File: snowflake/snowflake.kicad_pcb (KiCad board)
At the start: 2 copper layers, 150.2 x 150.2 mm, 82 parts, among them J1 Conn_01x05_Pin, J2 Conn_01x04_Pin, U1 TZ-5050S2RGB-5V-I4-H1, U10 TZ-5050S2RGB-5V-I4-H1, U11 TZ-5050S2RGB-5V-I4-H1, U12 TZ-5050S2RGB-5V-I4-H1, U13 TZ-5050S2RGB-5V-I4-H1, U14 TZ-5050S2RGB-5V-I4-H1, U15 TZ-5050S2RGB-5V-I4-H1, U16 TZ-5050S2RGB-5V-I4-H1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

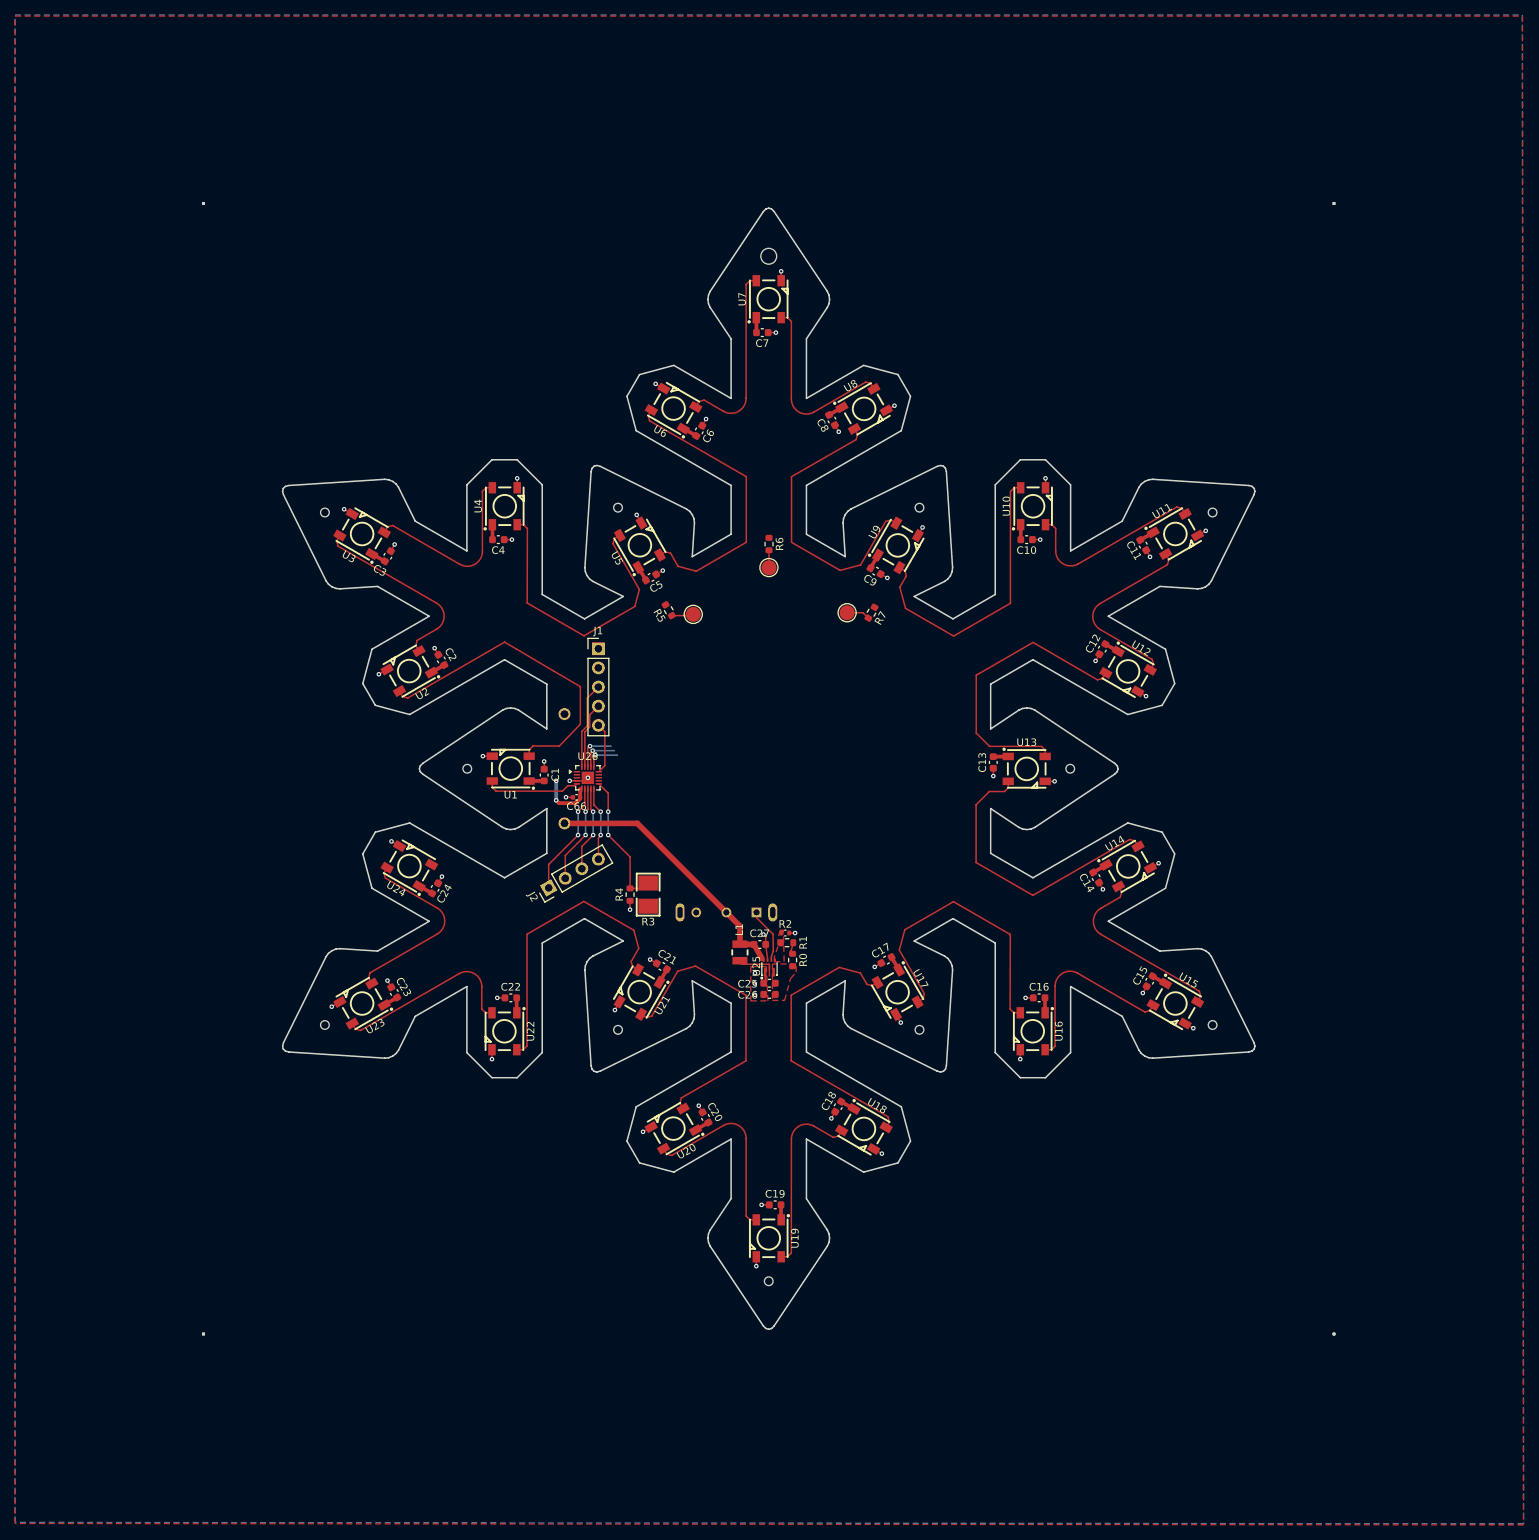
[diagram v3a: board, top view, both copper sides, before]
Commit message: Update PCB and customize some footprints
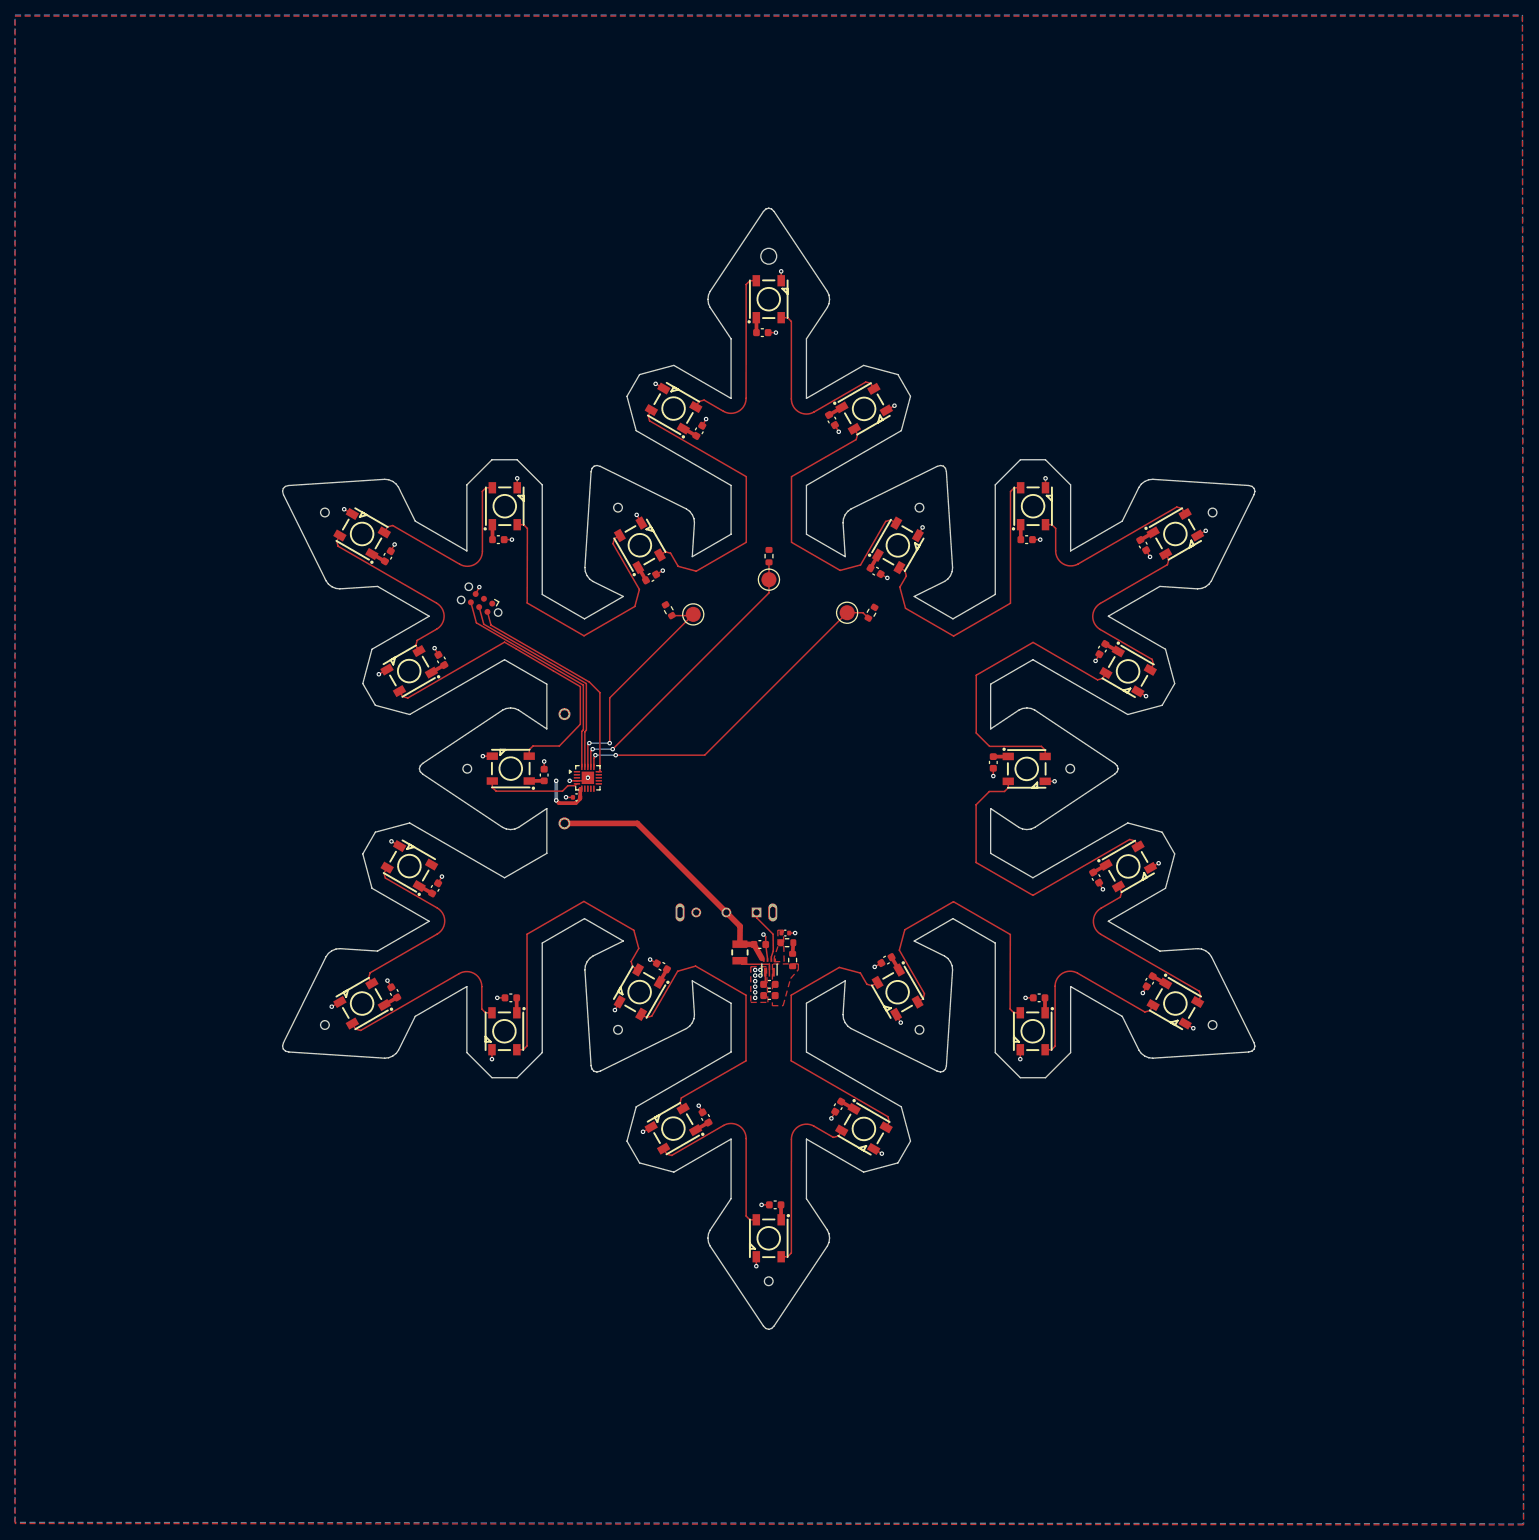
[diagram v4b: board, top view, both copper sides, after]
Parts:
- removed J1: Conn_01x05_Pin, Connector_PinHeader_2.54mm:PinHeader_1x05_P2.54mm_Vertical
- removed J2: Conn_01x04_Pin, Connector_PinHeader_2.54mm:PinHeader_1x04_P2.54mm_Vertical
- removed R3: C2904881, easyeda2kicad:RES-SMD_L3.6-W2.4
- removed R4: 10k, Resistor_SMD:R_0603_1608Metric
- added J3: TC2030, Connector:Tag-Connect_TC2030-IDC-NL_2x03_P1.27mm_Vertical, F.Cu at (111.9, 128.0)
- BAT1: footprint easyeda2kicad:BAT-TH_2P-P14.50_2462 -> snowflake:BAT-TH_2P-P14.50_2462
- C66: footprint Capacitor_SMD:C_0402_1005Metric -> snowflake:C_0402_1005Metric
- TP5, TP6, TP7: footprint TestPoint:TestPoint_Pad_D2.0mm -> snowflake:TestPoint_Pad_D2.0mm
- U25: footprint easyeda2kicad:VQFN-7_L2.0-W2.0-P0.55-TL_RWU -> snowflake:VQFN-7_L2.0-W2.0-P0.55-TL_RWU
- moved R6 1.60 mm to (150.0, 121.8)
- moved TP6 1.60 mm to (150.0, 124.9)
- moved C25 0.15 mm to (150.1, 178.6)
- moved C26 0.15 mm to (150.1, 180.1)
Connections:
- U26 pad 10: Net-(J2-Pin_4) -> unconnected-(U26-PC3/T1CH3-Pad10)
- U26 pad 11: /LDR_DIV -> unconnected-(U26-PC4/A2-Pad11)
- U26 pad 7: Net-(J2-Pin_1) -> unconnected-(U26-PC0/T2CH3-Pad7)
- U26 pad 8: Net-(J2-Pin_2) -> unconnected-(U26-PC1/SDA-Pad8)
- U26 pad 9: Net-(J2-Pin_3) -> unconnected-(U26-PC2/SCL-Pad9)
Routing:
- net /TOUCH3: track 7.33 -> 45.6 mm, vias 1 -> 2
- net /TOUCH2: track 8.28 -> 39.4 mm, vias 1 -> 2
- net /SWIO: track 6.84 -> 29.4 mm
- net /TOUCH1: track 8.64 -> 30.6 mm, vias 1 -> 2
- net /RX: track 8.80 -> 29.2 mm
- net /TX: track 11.5 -> 30.2 mm
- net /LDR_DIV: track 18.4 -> 0.00 mm, vias 2 -> 0
- net Net-(J2-Pin_1): track 15.1 -> 0.00 mm, vias 2 -> 0
- net Net-(J2-Pin_2): track 13.1 -> 0.00 mm, vias 2 -> 0
- net Net-(J2-Pin_3): track 11.4 -> 0.00 mm, vias 2 -> 0
- net Net-(J2-Pin_4): track 9.85 -> 0.00 mm, vias 2 -> 0
- net GND: track 65.4 -> 65.3 mm, vias 57 -> 62
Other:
- board size 150.2 x 150.2 mm -> 129 x 148.8 mm

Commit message: Add graphics to board
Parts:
- added J1: Conn_01x02_Pin, Connector_PinHeader_2.54mm:PinHeader_1x02_P2.54mm_Vertical, F.Cu at (123.2, 154.1)
- added REF**: front_silkscreen_text, snowflake:front_silkscreen_text, F.Cu at (149.7, 142.8)
- added REF**: front_silkscreen, snowflake:front_silkscreen, F.Cu at (150.2, 142.0)
- moved J3 46.5 mm to (134.5, 168.6), turned to -30 degrees
- moved R0 11.9 mm to (159.3, 165.2), turned to 180 degrees
- moved C26 10.9 mm to (157.0, 171.7)
- moved U25 10.9 mm to (157.0, 167.8)
- moved C25 10.9 mm to (157.0, 170.2)
- moved C27 10.9 mm to (155.7, 164.9)
- moved L1 10.9 mm to (153.1, 166.0)
- moved C66 10.6 mm to (127.7, 163.9), turned to 0 degrees
- moved R2 10.4 mm to (161.6, 167.3), turned to 90 degrees
- moved U26 10.3 mm to (128.0, 161.3)
- moved R1 9.48 mm to (160.1, 167.5), turned to -90 degrees
- moved S1 3.49 mm to (147.2, 171.2)
- moved R5 1.36 mm to (137.3, 130.2)
- moved R7 1.27 mm to (163.0, 130.4)
- moved TP6 1.09 mm to (150.0, 126.0)
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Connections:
- C1 pad 2: +5V -> Vdd
- C10 pad 2: +5V -> Vdd
- C11 pad 2: +5V -> Vdd
- C12 pad 2: +5V -> Vdd
- C13 pad 2: +5V -> Vdd
- C14 pad 2: +5V -> Vdd
- C15 pad 2: +5V -> Vdd
- C16 pad 2: +5V -> Vdd
- C17 pad 2: +5V -> Vdd
- C18 pad 2: +5V -> Vdd
- C19 pad 2: +5V -> Vdd
- C2 pad 2: +5V -> Vdd
- C20 pad 2: +5V -> Vdd
- C21 pad 2: +5V -> Vdd
- C22 pad 2: +5V -> Vdd
- C23 pad 2: +5V -> Vdd
- C24 pad 2: +5V -> Vdd
- C25 pad 1: +5V -> Vdd
- C26 pad 1: +5V -> Vdd
- C3 pad 2: +5V -> Vdd
- C4 pad 2: +5V -> Vdd
- C5 pad 2: +5V -> Vdd
- C6 pad 2: +5V -> Vdd
- C66 pad 1: +5V -> Vdd
- C7 pad 2: +5V -> Vdd
- C8 pad 2: +5V -> Vdd
- C9 pad 2: +5V -> Vdd
- J3 pad 1: +5V -> Vdd
- J3 pad 2: /SWIO -> /TX
- J3 pad 6: /TX -> /SWIO
- R0 pad 2: +5V -> /FB
- R1 pad 2: Net-(U25-FB) -> Vdd
- R2 pad 1: Net-(U25-FB) -> Vdd
- R5 pad 1: +5V -> Vdd
- R6 pad 1: +5V -> Vdd
- R7 pad 1: +5V -> Vdd
- S1 pad 1: /EN -> GND
- S1 pad 2: /BAT+ -> /EN
- S1 pad 3: unconnected-(S1-Pad3) -> /BAT+
- U1 pad 1: +5V -> Vdd
- U10 pad 1: +5V -> Vdd
- U11 pad 1: +5V -> Vdd
- U12 pad 1: +5V -> Vdd
- U13 pad 1: +5V -> Vdd
- U14 pad 1: +5V -> Vdd
- U15 pad 1: +5V -> Vdd
- U16 pad 1: +5V -> Vdd
- U17 pad 1: +5V -> Vdd
- U18 pad 1: +5V -> Vdd
- U19 pad 1: +5V -> Vdd
- U2 pad 1: +5V -> Vdd
- U20 pad 1: +5V -> Vdd
- U21 pad 1: +5V -> Vdd
- U22 pad 1: +5V -> Vdd
- U23 pad 1: +5V -> Vdd
- U24 pad 1: +5V -> Vdd
- U25 pad 3: +5V -> Vdd
- U25 pad 4: Net-(U25-FB) -> /FB
- U26 pad 6: +5V -> Vdd
- U3 pad 1: +5V -> Vdd
- U4 pad 1: +5V -> Vdd
- U5 pad 1: +5V -> Vdd
- U6 pad 1: +5V -> Vdd
- U7 pad 1: +5V -> Vdd
- U8 pad 1: +5V -> Vdd
- U9 pad 1: +5V -> Vdd
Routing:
- net +5V: track 55.4 -> 0.00 mm, vias 2 -> 0
- net Vdd: track 0.00 -> 49.0 mm
- net /SWIO: track 29.4 -> 11.3 mm
- net /TX: track 30.2 -> 14.8 mm, vias 0 -> 2
- net /RX: track 29.2 -> 15.3 mm, vias 0 -> 2
- net /DIN: track 12.7 -> 22.0 mm, vias 0 -> 1
- net /TOUCH3: track 45.6 -> 54.8 mm
- net /BAT+: track 35.4 -> 44.3 mm
- net /TOUCH2: track 39.4 -> 47.3 mm
- net /EN: track 7.10 -> 14.7 mm, vias 0 -> 2
- net /TOUCH1: track 30.6 -> 35.8 mm
- net GND: track 65.3 -> 68.8 mm, vias 62 -> 66
- net /FB: track 0.00 -> 2.06 mm
- net Net-(U1-DOU): track 42.1 -> 41.1 mm
- added copper zone on F.Cu, net Vdd
- removed copper zone on F.Cu, net +5V
- removed copper zone on F.Cu, net Net-(U25-FB)
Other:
- board text added: "off"
- board text added: "on"
